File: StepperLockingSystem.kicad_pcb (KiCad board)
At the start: 4 copper layers, 60 x 60 mm, 107 parts, among them J1 Phoenix Contact MSTB 4 Pin, J10 Conn_01x04_Male, J2 5Pin DuPont 2.54mm, J3 Molex PicoBlade 2Pin, J4 Molex PicoBlade 4Pin, J5 Molex PicoBlade 2Pin, J6 6Pin DuPont 2.56mm, J7 Molex PicoBlade 2Pin, J8 Molex PicoBlade 3Pin, J9 Molex PicoBlade 2Pin, Q1 IRLML0030, SW1 SW_Reset, U1 INA180A1, U2 TC1185, U3 24LC64, U4 STM32G0B1KET, U5 USBLC6-2SC6, U6 USBLC6-2SC6, U7 TMC2209-LA, Y1 ABM3B-16MHz

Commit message: Some changes to schematic
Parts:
- C1, C2, C3: value 100nF 35V -> 100nF
- C4, C6: value 1uF 35V -> 1uF
- C5: value 470pF 100V -> 470pF
- C7: value 100n -> 100nF
- F1: value 2A -> 12V 2A
- F2: value 2A -> 5V 2A
- J1: value Phoenix Contact MSTB 4 Pin -> PowerConnector
- J10: value Conn_01x04_Male -> Stepper
- J3: value Molex PicoBlade 2Pin -> Nerdstern
- J4: value Molex PicoBlade 4Pin -> HallEncoder
- J5: value Molex PicoBlade 2Pin -> MotorNTC
- J7: value Molex PicoBlade 2Pin -> DoorState
- J8: value Molex PicoBlade 3Pin -> OpenCloseButtons
- J9: value Molex PicoBlade 2Pin -> LockState
- J_LED1: value Molex PicoBlade -> DigitalLED
- R20: value 4.7k -> 4k7
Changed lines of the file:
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@@
       (effects (font (size 1 1) (thickness 0.15)))
     )
-    (fp_text value "Molex PicoBlade 2Pin" (at 0.62 2.35 90) (layer "F.Fab")
+    (fp_text value "LockState" (at 0.62 2.35 90) (layer "F.Fab")
       (effects (font (size 1 1) (thickness 0.15)))
     )
@@
       (effects (font (size 1 1) (thickness 0.15)) (justify right top))
     )
-    (fp_text value "2A" (at 10.1 -4.9) (layer "F.SilkS")
+    (fp_text value "12V 2A" (at 10.1 -4.9) (layer "F.SilkS")
       (effects (font (size 1 1) (thickness 0.15)) (justify right top))
     )
@@
       (effects (font (size 1 1) (thickness 0.15)))
     )
-    (fp_text value "1uF 35V" (at 0 1.43 90) (layer "F.Fab")
+    (fp_text value "1uF" (at 0 1.43 90) (layer "F.Fab")
       (effects (font (size 1 1) (thickness 0.15)))
     )
@@
       (effects (font (size 1 1) (thickness 0.15)))
     )
-    (fp_text value "Conn_01x04_Male" (at 3.75 4.6 90) (layer "F.Fab")
+    (fp_text value "Stepper" (at 3.75 4.6 90) (layer "F.Fab")
       (effects (font (size 1 1) (thickness 0.15)))
     )
@@
       (effects (font (size 1 1) (thickness 0.15)))
     )
-    (fp_text value "Molex PicoBlade" (at 1.88 2.35 90) (layer "F.Fab")
+    (fp_text value "DigitalLED" (at 1.88 2.35 90) (layer "F.Fab")
       (effects (font (size 1 1) (thickness 0.15)))
     )
@@
       (effects (font (size 1 1) (thickness 0.15)))
     )
-    (fp_text value "Molex PicoBlade 4Pin" (at 1.88 2.35 -270) (layer "F.Fab")
+    (fp_text value "HallEncoder" (at 1.88 2.35 -270) (layer "F.Fab")
       (effects (font (size 1 1) (thickness 0.15)))
     )
@@
       (effects (font (size 1 1) (thickness 0.15)))
     )
-    (fp_text value "100nF 35V" (at 0 1.43 90) (layer "F.Fab")
+    (fp_text value "100nF" (at 0 1.43 90) (layer "F.Fab")
       (effects (font (size 1 1) (thickness 0.15)))
     )
@@
       (effects (font (size 1 1) (thickness 0.15)))
     )
-    (fp_text value "Phoenix Contact MSTB 4 Pin" (at 7.62 5 90) (layer "F.Fab")
+    (fp_text value "PowerConnector" (at 7.62 5 90) (layer "F.Fab")
       (effects (font (size 1 1) (thickness 0.15)))
     )
@@
       (effects (font (size 1 1) (thickness 0.15)))
     )
-    (fp_text value "Molex PicoBlade 2Pin" (at 0.62 2.35) (layer "F.Fab")
+    (fp_text value "Nerdstern" (at 0.62 2.35) (layer "F.Fab")
       (effects (font (size 1 1) (thickness 0.15)))
     )
@@
       (effects (font (size 1 1) (thickness 0.15)))
     )
-    (fp_text value "470pF 100V" (at 0 1.43) (layer "F.Fab")
+    (fp_text value "470pF" (at 0 1.43) (layer "F.Fab")
       (effects (font (size 1 1) (thickness 0.15)))
     )
@@
       (effects (font (size 1 1) (thickness 0.15)) (justify right top))
     )
-    (fp_text value "2A" (at 10.1 -4.9) (layer "F.SilkS")
+    (fp_text value "5V 2A" (at 10.1 -4.9) (layer "F.SilkS")
       (effects (font (size 1 1) (thickness 0.15)) (justify right top))
     )
@@
       (effects (font (size 1 1) (thickness 0.15)))
     )
-    (fp_text value "Molex PicoBlade 2Pin" (at 0.62 2.35 90) (layer "F.Fab")
+    (fp_text value "DoorState" (at 0.62 2.35 90) (layer "F.Fab")
       (effects (font (size 1 1) (thickness 0.15)))
     )
@@
       (effects (font (size 1 1) (thickness 0.15)))
     )
-    (fp_text value "1uF 35V" (at 0 1.43 90) (layer "F.Fab")
+    (fp_text value "1uF" (at 0 1.43 90) (layer "F.Fab")
       (effects (font (size 1 1) (thickness 0.15)))
     )
@@
       (effects (font (size 1 1) (thickness 0.15)))
     )
-    (fp_text value "100nF 35V" (at 0 1.43 90) (layer "F.Fab")
+    (fp_text value "100nF" (at 0 1.43 90) (layer "F.Fab")
       (effects (font (size 1 1) (thickness 0.15)))
     )
@@
       (effects (font (size 1 1) (thickness 0.15)))
     )
-    (fp_text value "Molex PicoBlade 3Pin" (at 1.25 2.35 90) (layer "F.Fab")
+    (fp_text value "OpenCloseButtons" (at 1.25 2.35 90) (layer "F.Fab")
       (effects (font (size 1 1) (thickness 0.15)))
     )
@@
       (effects (font (size 1 1) (thickness 0.15)))
     )
-    (fp_text value "100nF 35V" (at 0 1.43 90) (layer "F.Fab")
+    (fp_text value "100nF" (at 0 1.43 90) (layer "F.Fab")
       (effects (font (size 1 1) (thickness 0.15)))
     )
@@
       (effects (font (size 1 1) (thickness 0.15)))
     )
-    (fp_text value "Molex PicoBlade 2Pin" (at 0.62 2.35) (layer "F.Fab")
+    (fp_text value "MotorNTC" (at 0.62 2.35) (layer "F.Fab")
       (effects (font (size 1 1) (thickness 0.15)))
     )
@@
       (effects (font (size 1 1) (thickness 0.15)) (justify mirror))
     )
-    (fp_text value "4.7k" (at 0 -1.43 90) (layer "B.Fab")
+    (fp_text value "4k7" (at 0 -1.43 90) (layer "B.Fab")
       (effects (font (size 1 1) (thickness 0.15)) (justify mirror))
     )
@@
       (effects (font (size 1 1) (thickness 0.15)) (justify mirror))
     )
-    (fp_text value "100n" (at 0 -1.43) (layer "B.Fab")
+    (fp_text value "100nF" (at 0 -1.43) (layer "B.Fab")
       (effects (font (size 1 1) (thickness 0.15)) (justify mirror))
     )
@@
     (pts (xy 185.05 79.95) (xy 125.05 79.95))
     (height 6.999999)
-    (gr_text "60.0000 mm" (at 155.05 72.95) (layer "Cmts.User")
+    (gr_text "60,0000 mm" (at 155.05 72.95) (layer "Cmts.User")
       (effects (font (size 1 1) (thickness 0.15)))
     )
@@
     (pts (xy 131.05 85.95) (xy 131.05 133.95))
     (height 14)
-    (gr_text "48.0000 mm" (at 117.05 109.95 90) (layer "Cmts.User")
+    (gr_text "48,0000 mm" (at 117.05 109.95 90) (layer "Cmts.User")
       (effects (font (size 1 1) (thickness 0.15)))
     )
@@
     (pts (xy 125.05 79.95) (xy 125.05 139.95))
     (height 12.000676)
-    (gr_text "60.0000 mm" (at 113.05 109.95 90) (layer "Cmts.User")
+    (gr_text "60,0000 mm" (at 113.05 109.95 90) (layer "Cmts.User")
       (effects (font (size 1 1) (thickness 0.15)))
     )
@@
     (pts (xy 131.05 85.95) (xy 179.05 85.95))
     (height -9)
-    (gr_text "48.0000 mm" (at 155.05 76.95) (layer "Cmts.User")
+    (gr_text "48,0000 mm" (at 155.05 76.95) (layer "Cmts.User")
       (effects (font (size 1 1) (thickness 0.15)))
     )

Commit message: Finish PCB layout
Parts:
- removed the TP2 at (207.0, 130.5)
- removed the TP3 at (215.1, 130.5)
- removed the TP8 at (215.1, 134.6)
- removed the TP9 at (219.2, 138.6)
- added C4: 180uF, Capacitor_THT:CP_Radial_D7.5mm_P2.50mm, F.Cu at (140.8, 67.7)
- added H3: MountingHole_Pad, extraFootprints:MountingHole_3.2mm_M3_ISO7380_Keepout, F.Cu at (171.0, 77.1)
- added TP5: TestPoint, TestPoint:TestPoint_Pad_D2.0mm, F.Cu at (150.1, 93.2)
- C19: renamed from C16; moved to B.Cu
- C20: renamed from C15; moved to B.Cu
- C5: renamed from C7; moved to F.Cu
- H1: footprint MountingHole:MountingHole_3.2mm_M3_ISO14580 -> extraFootprints:MountingHole_3.2mm_M3_ISO7380_Keepout
- H2: renamed from H7; footprint MountingHole:MountingHole_3.2mm_M3_ISO14580 -> extraFootprints:MountingHole_3.2mm_M3_ISO7380_Keepout
- H4: renamed from H2; footprint MountingHole:MountingHole_3.2mm_M3_ISO14580 -> extraFootprints:MountingHole_3.2mm_M3_ISO7380_Keepout
- H5: renamed from H6; footprint MountingHole:MountingHole_3.2mm_M3_ISO14580 -> extraFootprints:MountingHole_3.2mm_M3_ISO7380_Keepout
- H6: renamed from H5; footprint MountingHole:MountingHole_3.2mm_M3_ISO14580 -> extraFootprints:MountingHole_3.2mm_M3_ISO7380_Keepout
- H7: renamed from H3; footprint MountingHole:MountingHole_3.2mm_M3_ISO14580 -> extraFootprints:MountingHole_3.2mm_M3_ISO7380_Keepout
- H8: renamed from H4; footprint MountingHole:MountingHole_3.2mm_M3_ISO14580 -> extraFootprints:MountingHole_3.2mm_M3_ISO7380_Keepout
- J3: renamed from J8; value OpenCloseButtons -> Open+Close
- J4: renamed from J_SWD1; value Molex PicoBlade 6Pin -> SWD
- J5: renamed from J6; footprint Connector_PinHeader_2.54mm:PinHeader_1x07_P2.54mm_Vertical -> Connector_PinHeader_2.54mm:PinHeader_1x06_P2.54mm_Vertical
- R12: renamed from R11; moved to F.Cu
- R13: renamed from R14; moved to B.Cu
- R14: renamed from R15; moved to B.Cu
- R15: renamed from R16; moved to B.Cu
- R16: renamed from R13; moved to B.Cu
- R8: renamed from R5; moved to F.Cu
- R9: renamed from R6; moved to F.Cu
- SW1: value SW_Reset -> Reset
- U2: renamed from U3; moved to F.Cu
- U5: renamed from U6; moved to B.Cu
- U6: renamed from U5; moved to B.Cu
- moved H2 222.3 mm to (135.8, 77.1)
- moved H5 187.8 mm to (135.8, 101.1)
- moved J6 158.9 mm to (171.0, 84.0), turned to 0 degrees
- moved H6 156.3 mm to (171.0, 101.1)
- moved J12 115.0 mm to (169.4, 143.3), turned to 180 degrees
- moved R12 112.9 mm to (159.8, 140.6), turned to 0 degrees
- moved R13 108.6 mm to (126.6, 89.1), turned to -90 degrees
- moved R16 108.0 mm to (124.8, 89.1), turned to -90 degrees
- moved R9 106.9 mm to (162.3, 90.2)
- moved R8 106.1 mm to (162.3, 85.0)
- moved C18 104.0 mm to (144.5, 84.6), turned to 90 degrees
- moved C17 104.0 mm to (144.5, 87.8), turned to 90 degrees
- moved C20 103.9 mm to (129.6, 96.8), turned to 180 degrees
- moved C16 102.3 mm to (146.2, 87.8), turned to -90 degrees
- moved C15 102.3 mm to (146.5, 83.8), turned to -90 degrees
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- renumbered C8 to C1, C3 to C10, C2 to C11, C5 to C12, C4 to C13, C28 to C14, C17 to C15, C14 to C16, C18 to C17, C13 to C18, C10 to C2, C22 to C21, C21 to C22, C30 to C23, C23 to C24, C29 to C25, C32 to C26, C20 to C27, C31 to C28, C19 to C29, C9 to C3, C26 to C30, C27 to C31, C25 to C32, C34 to C33, C33 to C34, C24 to C35, C11 to C6, C1 to C7, C12 to C8, C6 to C9, D3 to D1, D4 to D2, D2 to D3, D1 to D4, F2 to F1, F1 to F2, J3 to J1, J5 to J10, J10 to J11, J4 to J12, J_LED1 to J2, J2 to J6, J9 to J7, J7 to J8, J1 to J9, R8 to R1, R1 to R10, R2 to R11, R20 to R17, R17 to R18, R21 to R19, R3 to R2, R19 to R20, R18 to R21, R24 to R22, R22 to R23, R23 to R24, R7 to R3, R12 to R5, R10 to R6, R9 to R7, TP4 to TP1, TP14 to TP10, TP10 to TP11, TP6 to TP2, TP5 to TP3, TP7 to TP4, TP1 to TP6, TP11 to TP7, TP12 to TP8, TP13 to TP9, U4 to U1, U2 to U3, U1 to U4
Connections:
- J5 pad 3: /MCU/PINB7 -> /MCU/PINB6
- J5 pad 4: /MCU/PINB8 -> /MCU/PINB7
- J5 pad 5: /MCU/PINB9 -> GND
- TP6 pad 1: /MCU/PINB2 -> /MCU/PINA7
- U1 pad 1: /MCU/PINB9 -> /MCU/CloseButton
- U1 pad 10: /MCU/Stepper_Diag -> /MCU/~{Stepper_Enable}
- U1 pad 11: /MCU/~{Stepper_Enable} -> /MCU/Stepper_Diag
- U1 pad 12: /MCU/PINA5 -> /MCU/Stepper_Step
- U1 pad 13: /MCU/PINA6 -> /MCU/Stepper_Direction
- U1 pad 14: /MCU/OpenButton -> /MCU/PINA7
- U1 pad 15: /MCU/CloseButton -> /MCU/PINB0
- U1 pad 16: /inputCurrent -> /MCU/tempMotor
- U1 pad 17: /MCU/PINB2 -> /inputCurrent
- U1 pad 18: /MCU/LockState -> unconnected-(U1-Pad18)
- U1 pad 20: /MCU/DoorState -> unconnected-(U1-Pad20)
- U1 pad 30: /MCU/Stepper_UART -> /MCU/PINB6
- U1 pad 32: /MCU/PINB8 -> /MCU/OpenButton
- U1 pad 7: /MCU/Stepper_Step -> /MCU/DoorState
- U1 pad 8: /MCU/tempMotor -> /MCU/LockState
- U1 pad 9: /MCU/Stepper_Direction -> /MCU/Stepper_UART
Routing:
- net +3V3: track 16.1 -> 209.7 mm, vias 2 -> 6
- net +5V: track 23.7 -> 172.6 mm, vias 0 -> 5
- net VCC: track 36.1 -> 161.1 mm, vias 14 -> 8
- net /MCU/I²C1_SCL: track 0.00 -> 74.4 mm, vias 0 -> 1
- net /MCU/I²C1_SDA: track 0.00 -> 71.2 mm, vias 0 -> 3
- net /MCU/Stepper_Step: track 0.00 -> 70.0 mm, vias 0 -> 3
- net /MCU/tempMotor: track 0.00 -> 69.4 mm, vias 0 -> 1
- net /MCU/~{Stepper_Enable}: track 22.9 -> 69.5 mm, vias 1 -> 3
- net /MCU/Stepper_Direction: track 27.5 -> 71.4 mm, vias 2 -> 3
- net /MCU/Stepper_Diag: track 21.8 -> 64.1 mm, vias 2 -> 3
- net /MCU/Stepper_UART: track 30.6 -> 63.1 mm
- net /MCU/LockState: track 2.28 -> 32.6 mm, vias 1 -> 3
- net /CAN/CAN_RX: track 0.00 -> 23.7 mm, vias 0 -> 1
- net Net-(D4-Pad1): track 28.3 -> 51.3 mm
- net /CAN/CAN_TX: track 0.00 -> 22.0 mm, vias 0 -> 1
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- added copper zone on In1.Cu, net GND
- added copper zone on In2.Cu, net GND
- removed copper zone on F.Cu, net Net-(F2-Pad1)
- removed copper zone on In1.Cu, net VCC
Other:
- board size 60 x 60 mm -> 54 x 84 mm
- rule pad_to_mask_clearance: 0 -> 0.05
- board text added: "Stepper-Locking-System v1.0 2022-05 by M. Grau"

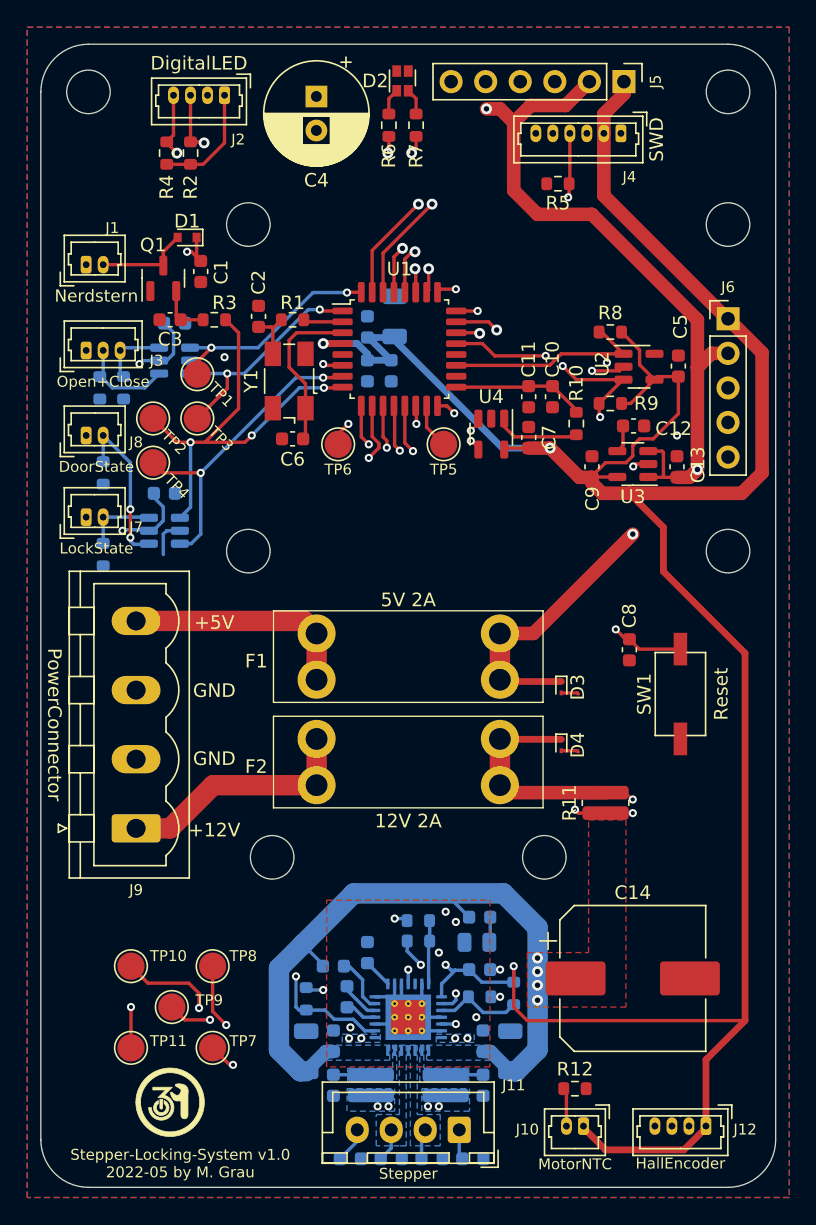
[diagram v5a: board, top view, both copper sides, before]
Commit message: Add ground plane vias
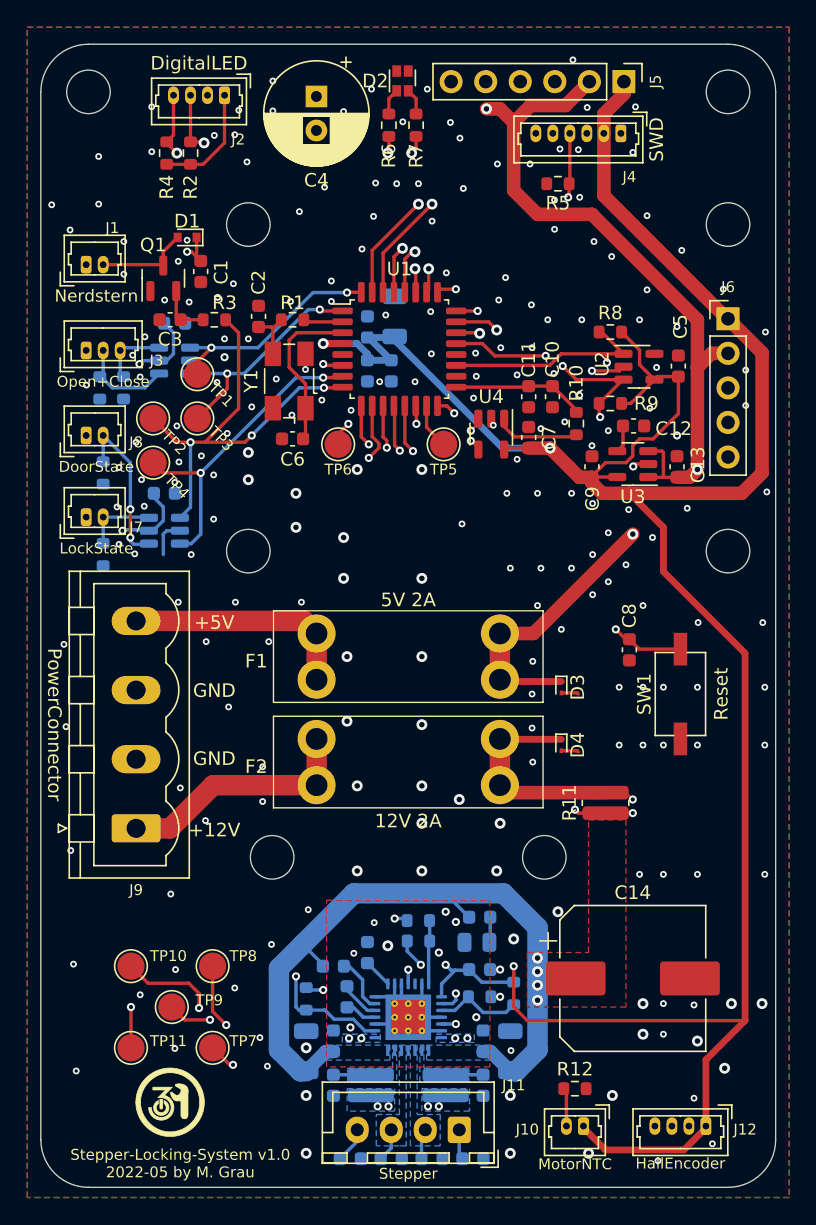
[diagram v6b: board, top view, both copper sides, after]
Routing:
- net GND: vias 15 -> 241

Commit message: Add BOM and update some values due component order
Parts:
- R13, R14, R15, R16: value 5k -> 5k6
- R23, R24: value 180m -> 150m
- R7: value 380R -> 390R
- R8, R9: value 2k -> 2k2
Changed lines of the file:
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@@
       (effects (font (size 1 1) (thickness 0.15)))
     )
-    (fp_text value "2k" (at 0 1.43) (layer "F.Fab")
+    (fp_text value "2k2" (at 0 1.43) (layer "F.Fab")
       (effects (font (size 1 1) (thickness 0.15)))
     )
@@
       (effects (font (size 1 1) (thickness 0.15)))
     )
-    (fp_text value "2k" (at 0 1.43) (layer "F.Fab")
+    (fp_text value "2k2" (at 0 1.43) (layer "F.Fab")
       (effects (font (size 1 1) (thickness 0.15)))
     )
@@
       (effects (font (size 1 1) (thickness 0.15)))
     )
-    (fp_text value "380R" (at 0 1.43 90) (layer "F.Fab")
+    (fp_text value "390R" (at 0 1.43 90) (layer "F.Fab")
       (effects (font (size 1 1) (thickness 0.15)))
     )
@@
       (effects (font (size 0.8 0.8) (thickness 0.15)) (justify mirror))
     )
-    (fp_text value "180m" (at 0 -2.65 90) (layer "B.Fab")
+    (fp_text value "150m" (at 0 -2.65 90) (layer "B.Fab")
       (effects (font (size 1 1) (thickness 0.15)) (justify mirror))
     )
@@
       (effects (font (size 1 1) (thickness 0.15)) (justify mirror))
     )
-    (fp_text value "5k" (at 0 -1.43 90) (layer "B.Fab")
+    (fp_text value "5k6" (at 0 -1.43 90) (layer "B.Fab")
       (effects (font (size 1 1) (thickness 0.15)) (justify mirror))
     )
@@
       (effects (font (size 0.8 0.8) (thickness 0.15)) (justify mirror))
     )
-    (fp_text value "180m" (at 0 -2.65 90) (layer "B.Fab")
+    (fp_text value "150m" (at 0 -2.65 90) (layer "B.Fab")
       (effects (font (size 1 1) (thickness 0.15)) (justify mirror))
     )
@@
       (effects (font (size 1 1) (thickness 0.15)) (justify mirror))
     )
-    (fp_text value "5k" (at 0 -1.43 90) (layer "B.Fab")
+    (fp_text value "5k6" (at 0 -1.43 90) (layer "B.Fab")
       (effects (font (size 1 1) (thickness 0.15)) (justify mirror))
     )
@@
       (effects (font (size 1 1) (thickness 0.15)) (justify mirror))
     )
-    (fp_text value "5k" (at 0 -1.43 90) (layer "B.Fab")
+    (fp_text value "5k6" (at 0 -1.43 90) (layer "B.Fab")
       (effects (font (size 1 1) (thickness 0.15)) (justify mirror))
     )
@@
       (effects (font (size 1 1) (thickness 0.15)) (justify mirror))
     )
-    (fp_text value "5k" (at 0 -1.43 90) (layer "B.Fab")
+    (fp_text value "5k6" (at 0 -1.43 90) (layer "B.Fab")
       (effects (font (size 1 1) (thickness 0.15)) (justify mirror))
     )
